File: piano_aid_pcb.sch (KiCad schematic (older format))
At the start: 20 parts

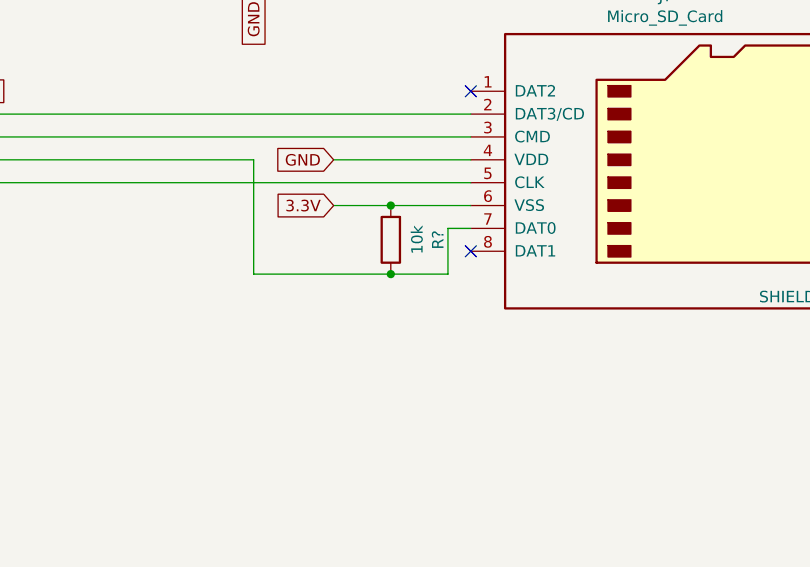
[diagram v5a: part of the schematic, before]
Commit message: Added sdcard pull up to unused pin per kingston specifications
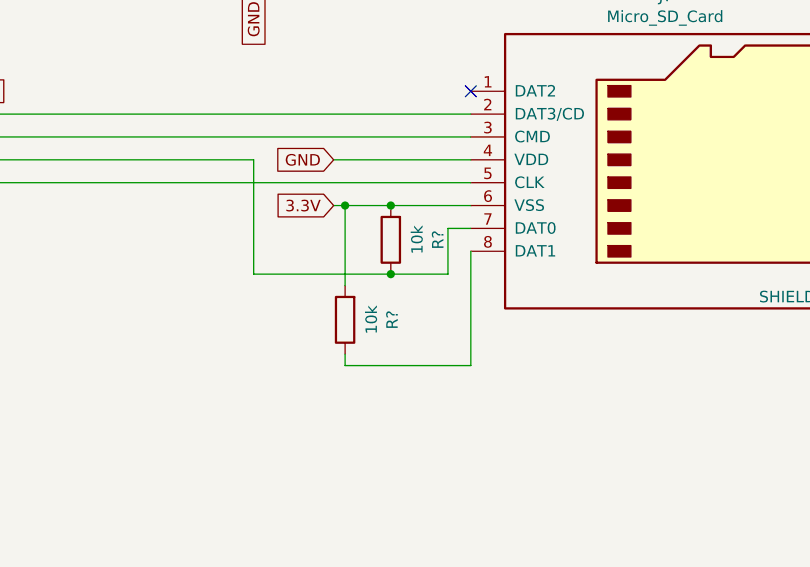
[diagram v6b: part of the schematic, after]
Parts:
- added R?: 10k, symbol Device:R
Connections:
- net 3.3V: now also R?.2
- net at J?.8 (DAT1): now also R?.1
- no-connect marks 4 -> 3
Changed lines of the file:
@@
 	8650 4000 9250 4000
 Wire Wire Line
-	8650 4200 8900 4200
+	8650 4200 8700 4200
 Connection ~ 8900 4200
 Wire Wire Line
 	9250 3800 5650 3800
-NoConn ~ 9250 4400
 NoConn ~ 9250 3700
 Wire Wire Line
@@
 Wire Wire Line
 	3250 6600 3250 7000
+Wire Wire Line
+	8700 4200 8700 4550
+Connection ~ 8700 4200
+Wire Wire Line
+	8700 4200 8900 4200
+$Comp
+L Device:R R?
+U 1 1 6146BED1
+P 8700 4700
+F 0 "R?" V 8493 4700 50  0000 C CNN
+F 1 "10k" V 8584 4700 50  0000 C CNN
+F 2 "" V 8630 4700 50  0001 C CNN
+F 3 "~" H 8700 4700 50  0001 C CNN
+	1    8700 4700
+	-1   0    0    1
+$EndComp
+Wire Wire Line
+	8700 4900 9250 4900
+Wire Wire Line
+	9250 4400 9250 4900
+Wire Wire Line
+	8700 4900 8700 4850
 $EndSCHEMATC
